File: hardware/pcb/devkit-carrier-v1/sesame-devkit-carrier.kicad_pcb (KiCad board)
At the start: 2 copper layers, 69 x 42 mm, 24 parts, among them J1 DevKit L, J2 DevKit R, J3 OLED, J4 IO, J5 IO2, J6 Battery pigtail, SW1 Switch, U1 Pololu D24V50F5

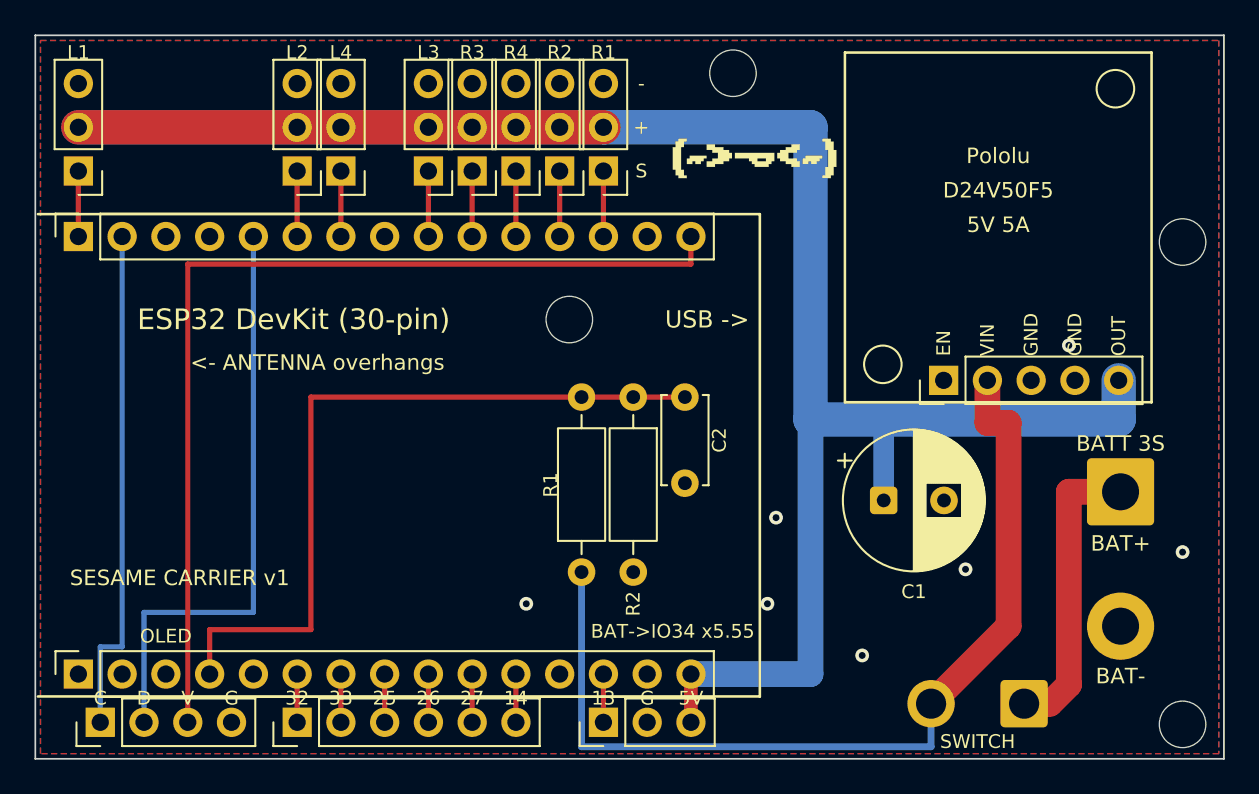
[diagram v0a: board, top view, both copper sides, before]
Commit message: Carrier PCB: full audit pass, clean DRC, regulator input cap
- Add C3 (47 uF 35 V) across the regulator input per Pololu's LC-spike
  app note; 5 mm part so it clears the DevKit's USB end.
- DRC now 0 violations: per-header silkscreen moved to Fab with one
  outline per header group, label collisions fixed, silkscreen lines
  lifted to PCBWay's 0.15 mm minimum, and deliberate side-by-side
  header courtyards allowed in a documented .kicad_dru rule.
- audit.py extended: C3, capacitor voltage ratings, PCBWay limits, real
  header spacing. README lists every documentation source checked.

Co-Authored-By: Claude Opus 5.5 <noreply@anthropic.com>
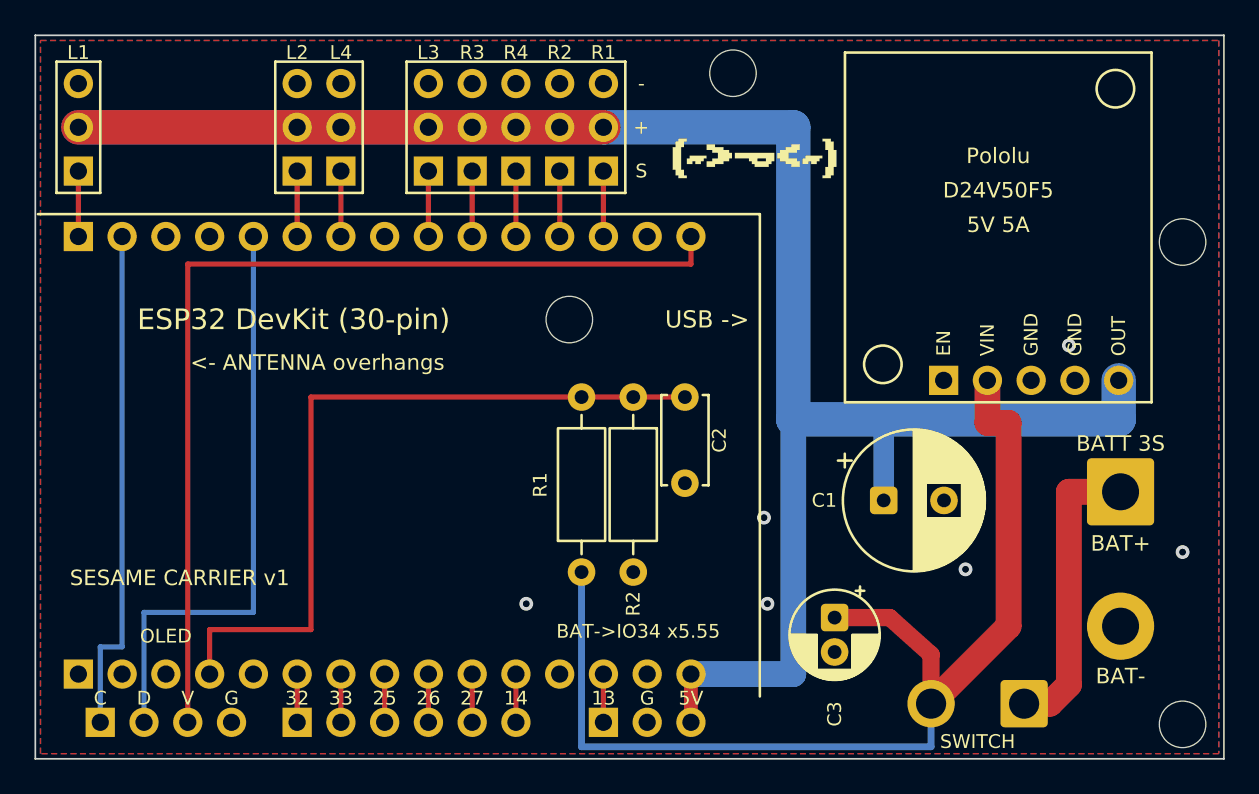
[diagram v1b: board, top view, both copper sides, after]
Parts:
- added C3: 47uF 35V, CP_Radial_D5.0mm_P2.00mm, F.Cu at (46.4, 33.8)
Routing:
- net VBAT_SW: track 54.8 -> 64.1 mm
- net +5V: track 139.3 -> 138.3 mm
- net GND: vias 7 -> 6

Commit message: Carrier PCB: mounting holes at all four corners
Add top-left and bottom-left holes (threaded between the left-end traces)
and move the right hole to the top-right corner, so the DevKit end no
longer cantilevers when servos, the OLED or the DevKit are pushed on.

Co-Authored-By: Claude Opus 5.5 <noreply@anthropic.com>
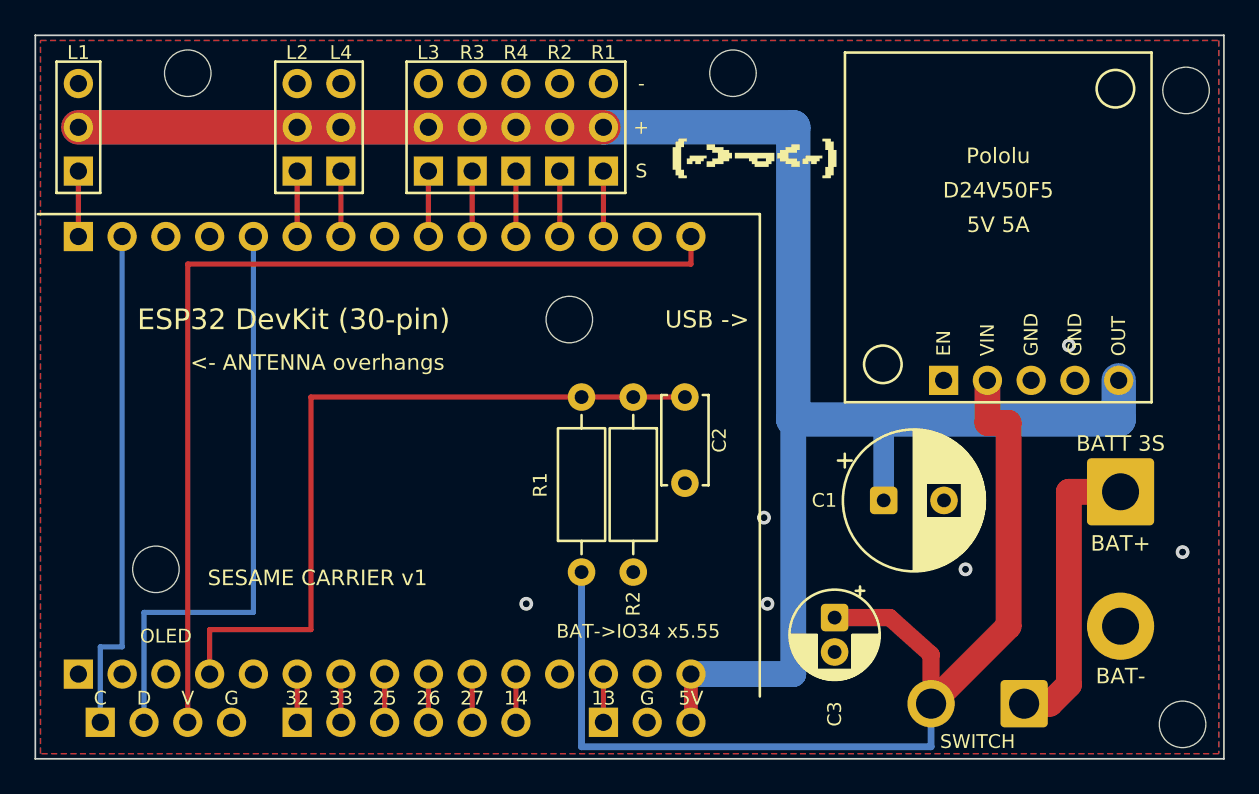
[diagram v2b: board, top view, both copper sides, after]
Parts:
- added H5: MountingHole_2.7mm_M2.5, MountingHole_2.7mm_M2.5, F.Cu at (66.8, 3.20)
- added H6: MountingHole_2.7mm_M2.5, MountingHole_2.7mm_M2.5, F.Cu at (66.6, 40.0)
- moved H2 62.6 mm to (7.00, 31.0)
- moved H3 45.9 mm to (40.5, 2.20)
- moved H1 31.6 mm to (8.85, 2.20)

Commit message: Carrier PCB: 3 mm screw-head keep-out around every mounting hole
Only ground fill may sit under a screw head. Servo 5V rail dips around the
top-left hole, the regulator feed comes in below the servo headers instead
of past the top-middle hole, and SDA is rerouted so the bottom-left hole
gets its own clear column at (12.4, 31). Keep-out rule areas make DRC
enforce it; audit.py checks the distance to every non-GND copper item.

Co-Authored-By: Claude Opus 5.5 <noreply@anthropic.com>
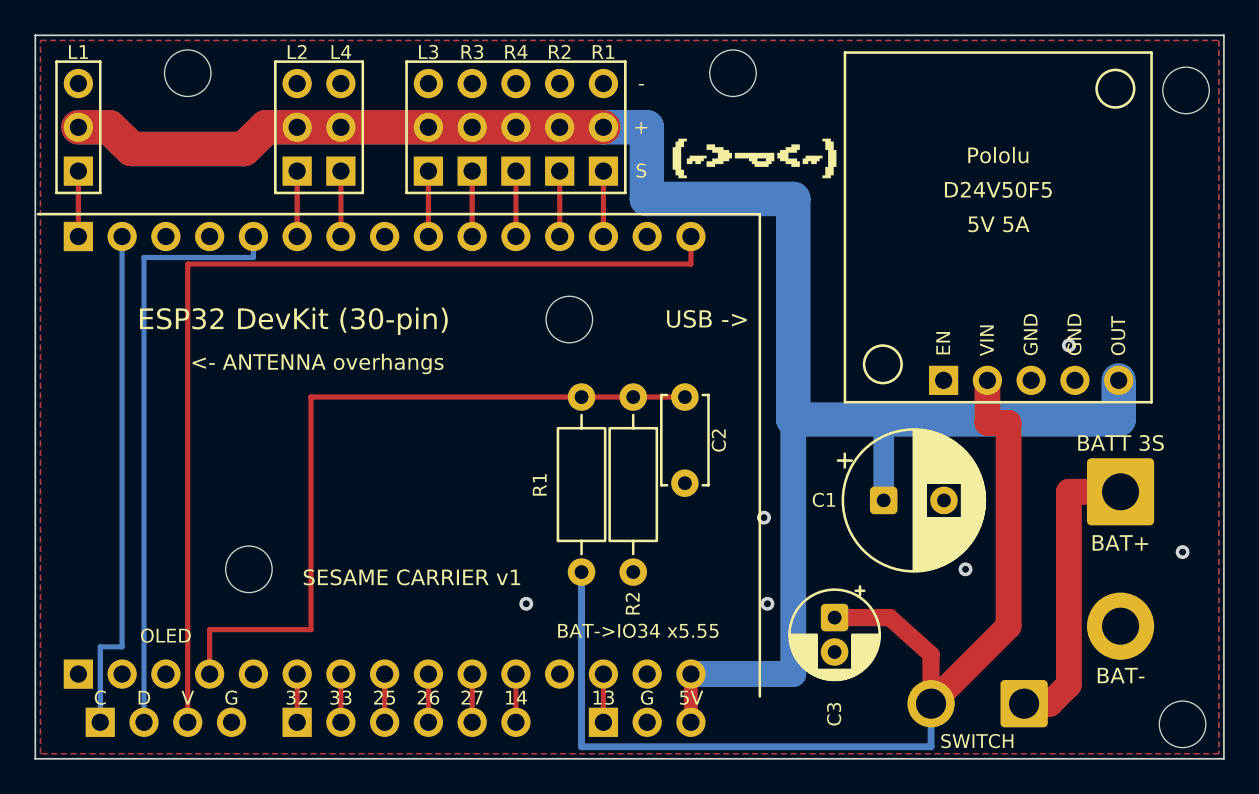
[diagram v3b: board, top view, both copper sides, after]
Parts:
- moved H2 5.40 mm to (12.4, 31.0)
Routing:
- net +5V: track 138.3 -> 140.4 mm

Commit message: Carrier PCB: Pololu-matched M2 holes, bottom-left hole near edge
- Add M2 holes (HP1/HP2) under the Pololu module's own mounting holes so a
  screw can clamp module, printed standoff and carrier; drop the top-right
  M2.5 hole that sat under the module's corner.
- Reroute SCL off the far left so the bottom-left hole moves to (3.8, 30).
- Regulator 5V output steps clear of HP1 (M2 keep-out 2.4 mm).
- Remove the 'ANTENNA overhangs' and 'USB' silkscreen labels.

Co-Authored-By: Claude Opus 5.5 <noreply@anthropic.com>
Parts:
- removed H6: MountingHole_2.7mm_M2.5, MountingHole_2.7mm_M2.5
- added HP1: MountingHole_2.2mm_M2, MountingHole_2.2mm_M2, F.Cu at (49.2, 19.1)
- added HP2: MountingHole_2.2mm_M2, MountingHole_2.2mm_M2, F.Cu at (62.7, 3.10)
- moved H5 36.8 mm to (66.6, 40.0)
- moved H2 8.66 mm to (3.80, 30.0)
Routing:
- net SCL: track 29.5 -> 40.4 mm
- net +5V: track 140.4 -> 139.7 mm
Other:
- board text removed: "<- ANTENNA overhangs"
- board text removed: "USB ->"

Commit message: Carrier PCB: label DevKit area ESP-WROOM-32, drop front title
Co-Authored-By: Claude Opus 5.5 <noreply@anthropic.com>
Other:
- board text added: "ESP-WROOM-32"
- board text removed: "ESP32 DevKit (30-pin)"
- board text removed: "SESAME CARRIER v1"

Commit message: Carrier PCB: generated schematic, ERC and schematic/PCB parity
- gen_schematic.py builds sesame-devkit-carrier.kicad_sch from the board,
  with named, electrically typed pins for the DevKit rows and the Pololu
  (Sesame.kicad_sym), power flags, and no-connects on unused pins.
- Footprints now come from the project library Sesame.pretty (stock
  footprints with the silkscreen tweaks baked in), so the board matches its
  library; footprints link to their symbols; unused pads carry KiCad's
  unconnected-(...) nets. Project sym/fp lib tables make it self-contained.
- ERC 0/0, DRC with schematic parity 0 violations / 0 footprint errors,
  schematic netlist matches all 86 board pads, audit.py passes.

Co-Authored-By: Claude Opus 5.5 <noreply@anthropic.com>
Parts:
- C1: footprint CP_Radial_D8.0mm_P3.50mm -> Sesame:CP_Radial_D8.0mm_P3.50mm
- C2: footprint C_Disc_D5.0mm_W2.5mm_P5.00mm -> Sesame:C_Disc_D5.0mm_W2.5mm_P5.00mm
- C3: footprint CP_Radial_D5.0mm_P2.00mm -> Sesame:CP_Radial_D5.0mm_P2.00mm
- H1, H2, H3, H4, H5: footprint MountingHole_2.7mm_M2.5 -> Sesame:MountingHole_2.7mm_M2.5
- HP1, HP2: footprint MountingHole_2.2mm_M2 -> Sesame:MountingHole_2.2mm_M2
- J1, J2: footprint PinSocket_1x15_P2.54mm_Vertical -> Sesame:PinSocket_1x15_P2.54mm_Vertical_GroupSilk
- J3: footprint PinHeader_1x04_P2.54mm_Vertical -> Sesame:PinHeader_1x04_P2.54mm_Vertical_GroupSilk
- J4: footprint PinHeader_1x06_P2.54mm_Vertical -> Sesame:PinHeader_1x06_P2.54mm_Vertical_GroupSilk
- J5, S1, S2, S3, S4, S5, S6, S7, S8: footprint PinHeader_1x03_P2.54mm_Vertical -> Sesame:PinHeader_1x03_P2.54mm_Vertical_GroupSilk
- J6: footprint SolderWire-1.5sqmm_1x02_P7.8mm_D1.7mm_OD3.9mm -> Sesame:SolderWire-1.5sqmm_1x02_P7.8mm_D1.7mm_OD3.9mm
- R1, R2: footprint R_Axial_DIN0207_L6.3mm_D2.5mm_P10.16mm_Horizontal -> Sesame:R_Axial_DIN0207_L6.3mm_D2.5mm_P10.16mm_Horizontal
- SW1: footprint SolderWire-1sqmm_1x02_P5.4mm_D1.4mm_OD2.7mm -> Sesame:SolderWire-1sqmm_1x02_P5.4mm_D1.4mm_OD2.7mm
- U1: footprint PinHeader_1x05_P2.54mm_Vertical -> Sesame:PinHeader_1x05_P2.54mm_Vertical_GroupSilk
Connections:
- J1 pad 1: (no net) -> unconnected-(J1-EN-Pad1)
- J1 pad 12: (no net) -> unconnected-(J1-D12-Pad12)
- J1 pad 2: (no net) -> unconnected-(J1-VP-Pad2)
- J1 pad 3: (no net) -> unconnected-(J1-VN-Pad3)
- J1 pad 5: (no net) -> unconnected-(J1-D35-Pad5)
- J2 pad 3: (no net) -> unconnected-(J2-TX0-Pad3)
- J2 pad 4: (no net) -> unconnected-(J2-RX0-Pad4)
- J2 pad 8: (no net) -> unconnected-(J2-D5-Pad8)
- U1 pad 1: (no net) -> unconnected-(U1-EN-Pad1)

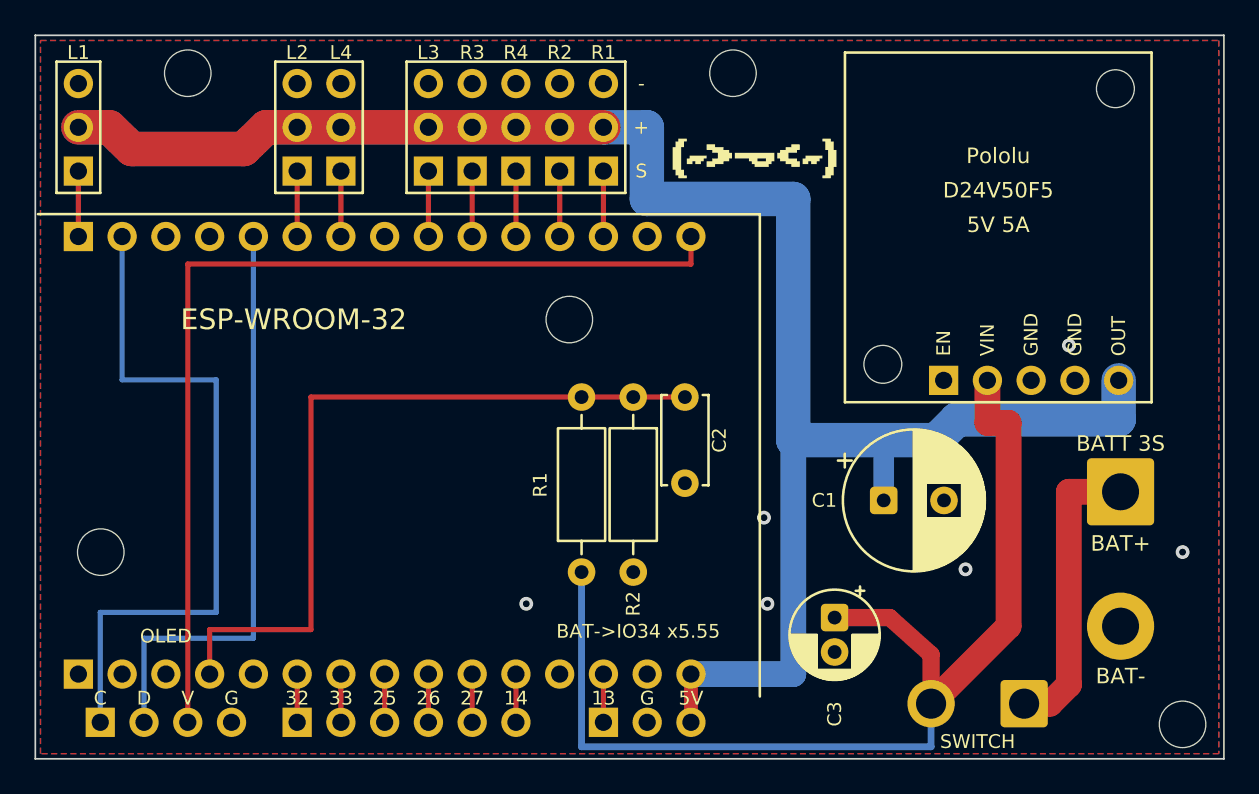
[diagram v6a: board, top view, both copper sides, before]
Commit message: Carrier PCB: kicad-happy review, pan-head edge clearance for M2.5 holes
kicad-happy flagged H5's courtyard past the board edge; root cause was
sizing holes for a 4.5 mm socket head instead of a 5.0 mm pan head. H1, H3
and H5 moved to >= 2.95 mm from the edge, servo rail dip lowered to keep
H1's 3 mm copper keep-out, battery pads shifted up 1 mm. audit.py checks
pan-head edge clearance. REVIEW.md records every kicad-happy finding and
its disposition.

Co-Authored-By: Claude Opus 5.5 <noreply@anthropic.com>
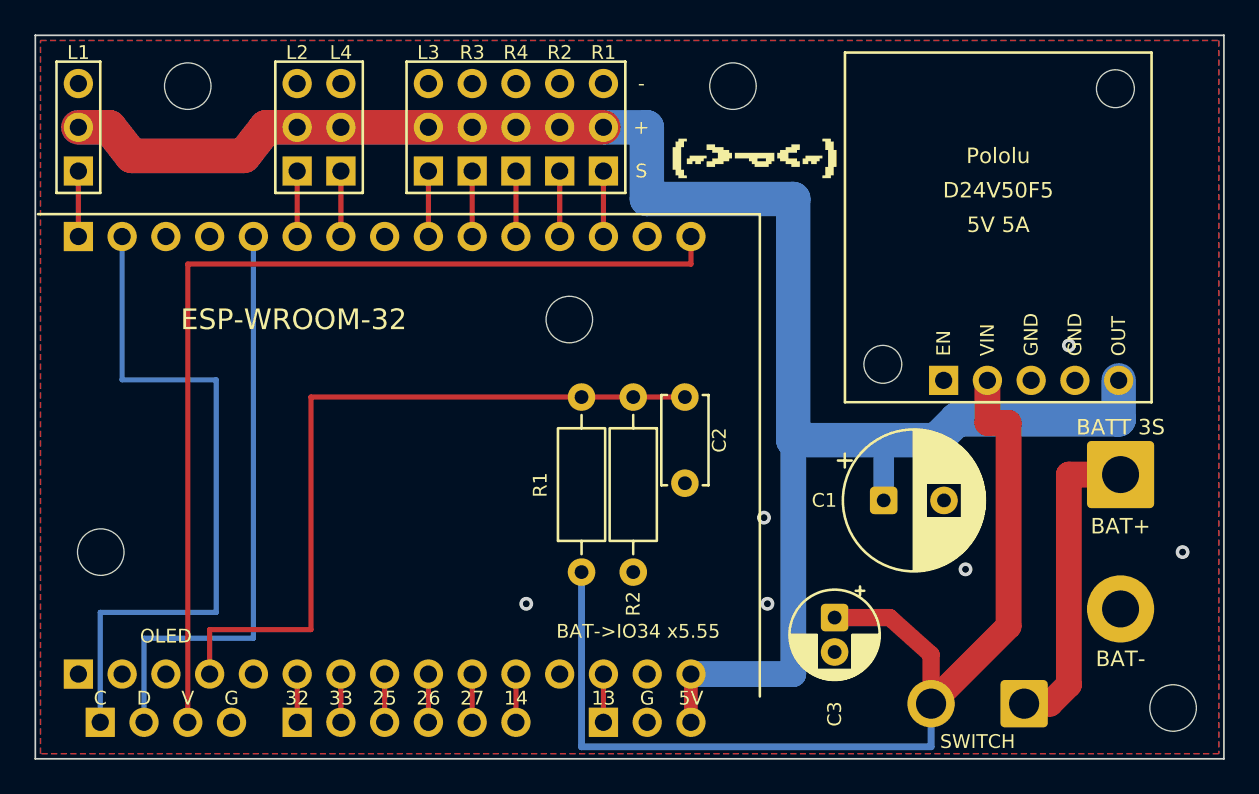
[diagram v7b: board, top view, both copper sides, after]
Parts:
- moved H5 1.10 mm to (66.0, 39.0)
- moved J6 1.00 mm to (63.0, 25.5)
- moved H1 0.75 mm to (8.85, 2.95)
- moved H3 0.75 mm to (40.5, 2.95)
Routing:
- net +5V: track 139.7 -> 140.9 mm
- net VBAT: track 17.3 -> 18.3 mm
